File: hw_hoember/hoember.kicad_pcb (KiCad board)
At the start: 2 copper layers, 27.9 x 55 mm, 42 parts, among them J1 Conn_2Rows-05Pins, Q1 AO3401A, Q2 AO3401A, Q3 AO3401A, SW1 SW_DPST_x2, T1 Tab, U1 PY32F002AF15P6TU

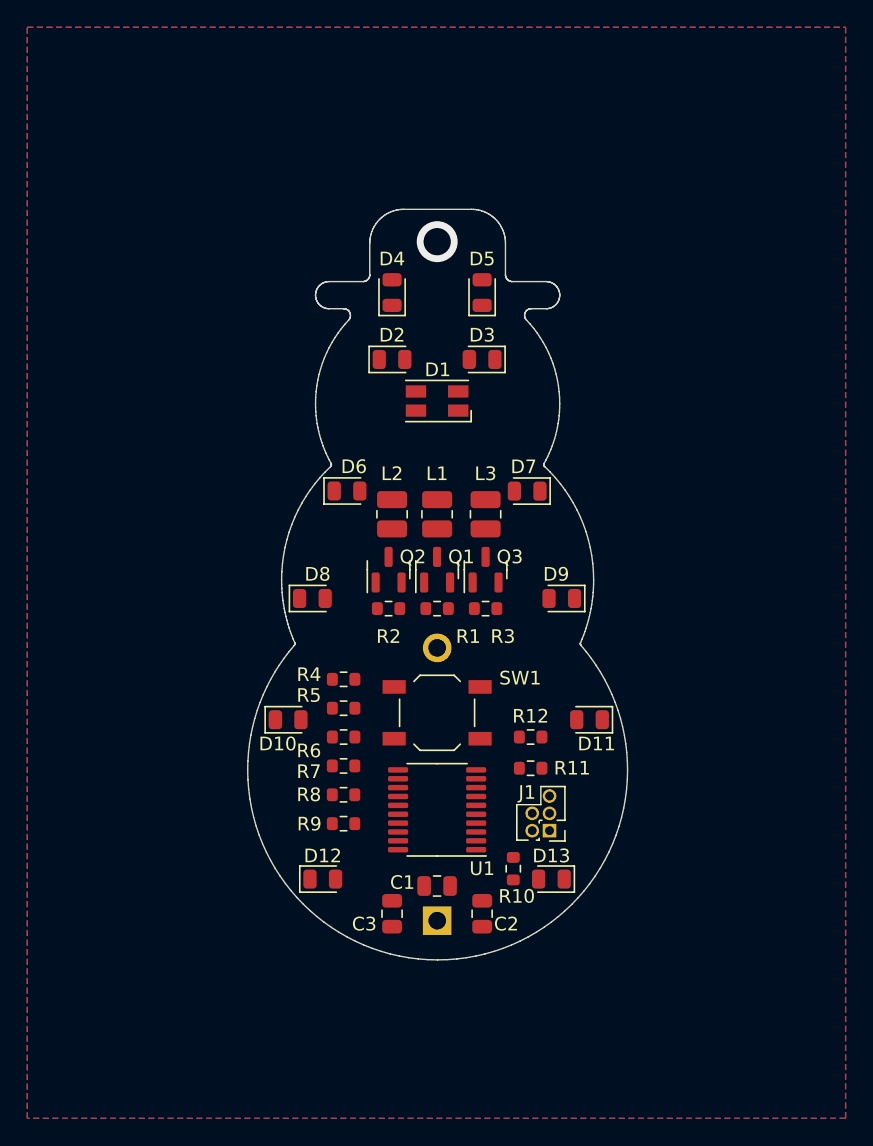
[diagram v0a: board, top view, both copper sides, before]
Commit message: Hoember + Mezi routed
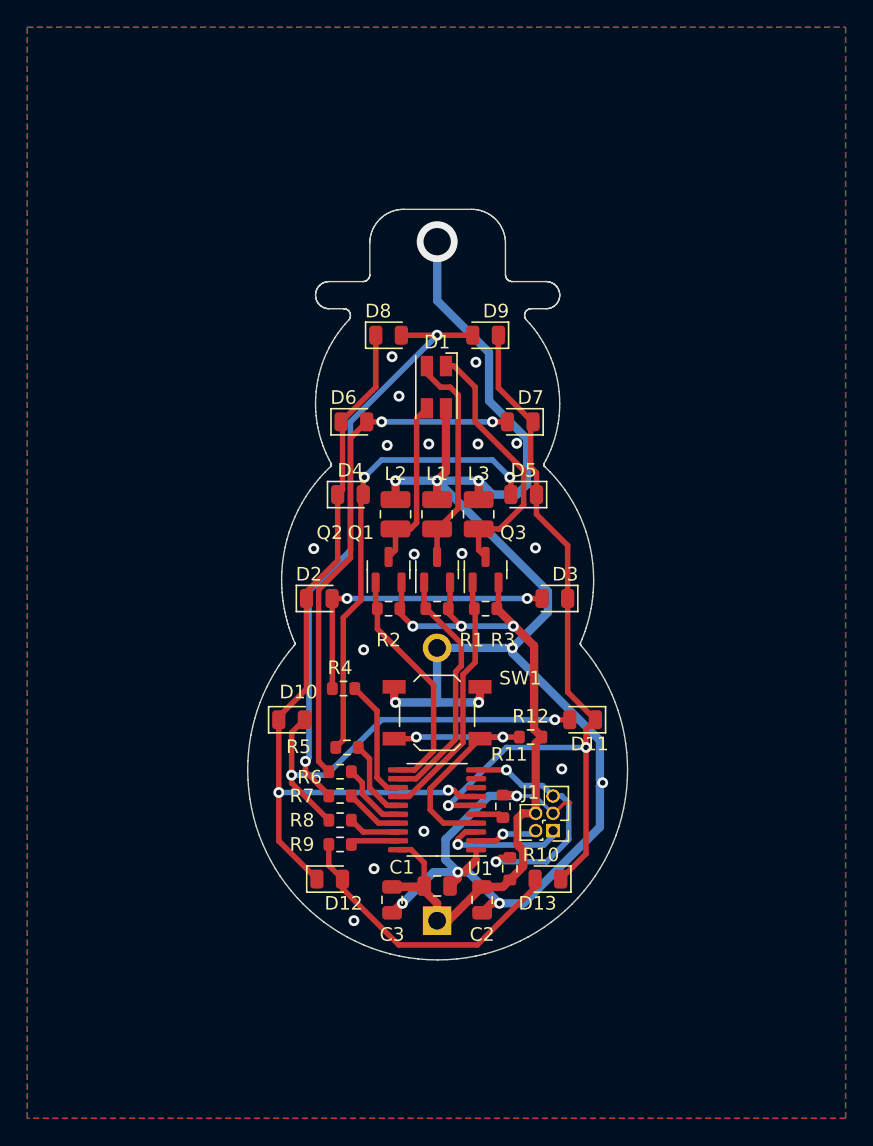
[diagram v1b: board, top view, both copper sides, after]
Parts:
- moved D8 20.1 mm to (126.5, 52.6)
- moved D9 20.1 mm to (133.6, 52.6)
- moved D3 18.3 mm to (138.7, 71.9)
- moved D2 18.3 mm to (121.4, 71.9)
- moved D4 15.1 mm to (123.7, 64.3), turned to 0 degrees
- moved D5 15.1 mm to (136.4, 64.3), turned to 180 degrees
- moved D7 5.11 mm to (136.1, 58.9)
- moved D6 5.10 mm to (124.0, 58.9)
- moved R11 3.45 mm to (134.9, 87.1), turned to -90 degrees
- moved R5 2.89 mm to (123.4, 82.8)
- moved R6 2.55 mm to (122.9, 84.6)
- moved R7 2.22 mm to (122.9, 86.4)
- moved R8 1.88 mm to (122.9, 88.1)
- moved R9 1.55 mm to (122.9, 89.9)
- moved D1 1.02 mm to (130.0, 56.4), turned to -90 degrees
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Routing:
- net GND: track 0.00 -> 131.7 mm, vias 1 -> 28
- net /MPX2: track 0.00 -> 59.0 mm, vias 0 -> 2
- net /MPX1: track 0.00 -> 58.3 mm, vias 0 -> 2
- net VCC: track 0.00 -> 58.1 mm, vias 0 -> 3
- net Net-(D8-A): track 0.00 -> 43.8 mm, vias 0 -> 2
- net Net-(D6-A): track 0.00 -> 38.0 mm, vias 0 -> 2
- net Net-(D4-A): track 0.00 -> 33.8 mm, vias 0 -> 2
- net Net-(D10-A): track 0.00 -> 31.2 mm, vias 0 -> 2
- net Net-(D2-A): track 0.00 -> 22.4 mm, vias 0 -> 2
- net Net-(D12-A): track 0.00 -> 21.8 mm
- net Net-(SW1A-A): track 0.00 -> 21.5 mm, vias 0 -> 2
- net Net-(D1-GK): track 0.00 -> 19.2 mm
- net /G: track 0.00 -> 18.6 mm
- net /B: track 0.00 -> 18.2 mm
- net /nRST: track 0.00 -> 17.6 mm, vias 0 -> 2
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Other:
- board text added: "PCB by Olivér & Kristóf"
- board text removed: "PCB by Dávid & Kristóf"
